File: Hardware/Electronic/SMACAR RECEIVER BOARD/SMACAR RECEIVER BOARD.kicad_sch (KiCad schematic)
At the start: 7 parts, among them J1 M04POLAR, J2 USB_C_Receptacle_USB2.0_14P, U1 ESP32-S3-DevKitC

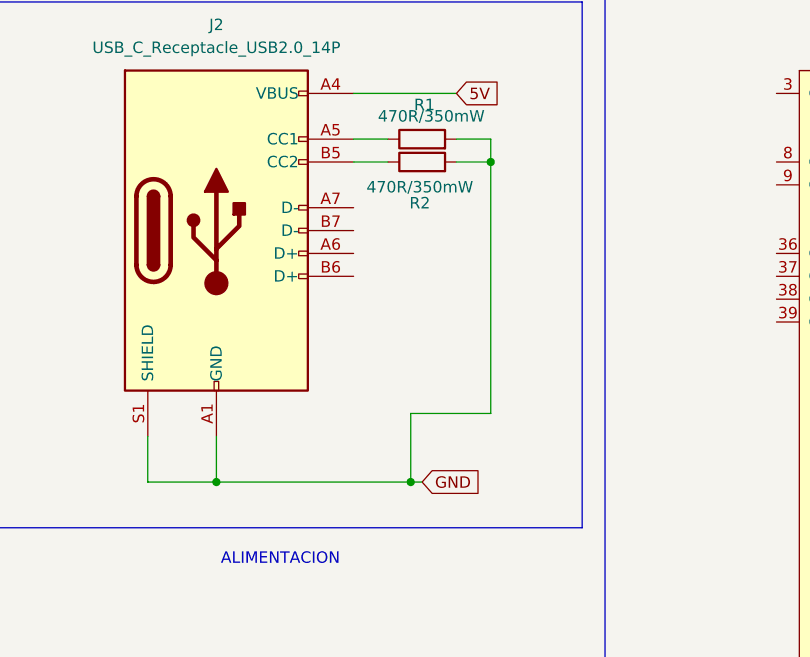
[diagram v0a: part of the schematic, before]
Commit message: arreglos en las conexiones de usb c
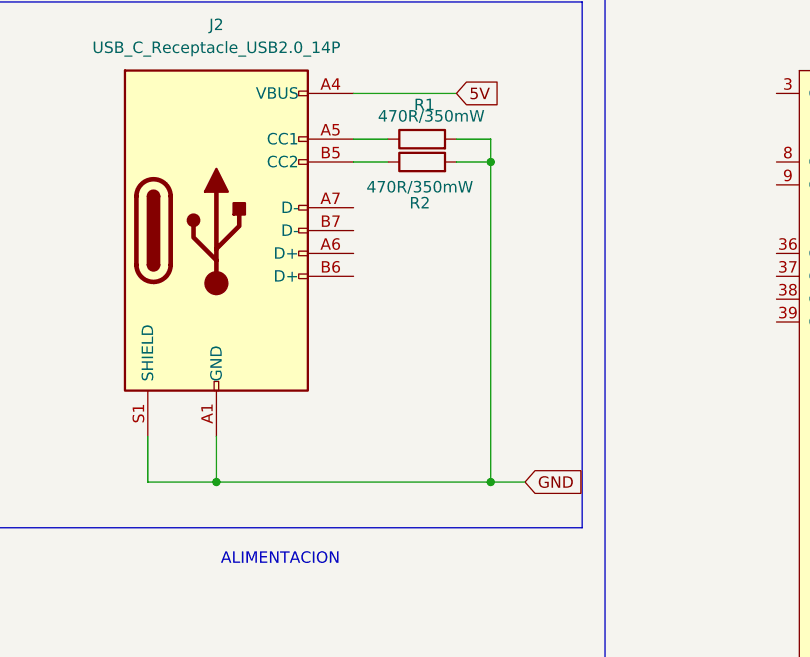
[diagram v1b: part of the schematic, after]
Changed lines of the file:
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@@
+	)
+	(junction
+		(at 86.36 71.12)
+		(diameter 0)
+		(color 0 0 0 0)
 	)
 	(junction
@@
 	)
 	(junction
-		(at 77.47 71.12)
-		(diameter 0)
-		(color 0 0 0 0)
-	)
-	(junction
 		(at 186.69 73.66)
 		(diameter 0)
@@
 	(wire
 		(pts
-			(xy 77.47 71.12) (xy 77.47 63.5)
+			(xy 86.36 35.56) (xy 86.36 71.12)
 		)
 		(stroke
@@
 	(wire
 		(pts
-			(xy 55.88 71.12) (xy 77.47 71.12)
+			(xy 55.88 71.12) (xy 86.36 71.12)
 		)
 		(stroke
@@
 	(wire
 		(pts
-			(xy 77.47 71.12) (xy 78.74 71.12)
-		)
-		(stroke
-			(width 0)
-			(type default)
-		)
-	)
-	(wire
-		(pts
 			(xy 86.36 33.02) (xy 82.55 33.02)
 		)
@@
 	(wire
 		(pts
-			(xy 77.47 63.5) (xy 86.36 63.5)
-		)
-		(stroke
-			(width 0)
-			(type default)
-		)
-	)
-	(wire
-		(pts
 			(xy 144.78 22.86) (xy 144.78 20.32)
 		)
@@
 	(wire
 		(pts
-			(xy 86.36 63.5) (xy 86.36 35.56)
+			(xy 86.36 71.12) (xy 90.17 71.12)
 		)
 		(stroke
@@
 	(global_label "GND"
 		(shape input)
-		(at 78.74 71.12 0)
+		(at 90.17 71.12 0)
 		(fields_autoplaced yes)
 		(effects
@@
 		)
 		(property "Intersheetrefs" "${INTERSHEET_REFS}"
-			(at 85.5957 71.12 0)
+			(at 97.0257 71.12 0)
 			(effects
 				(font

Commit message: TVS
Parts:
- added U2, U3: TVS0500DRV, Package_SON:WSON-6-1EP_2x2mm_P0.65mm_EP1x1.6mm, symbol Power_Protection:TVS0500DRV
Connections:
- net 5V: now also U2.4 (IN), U2.5 (IN), U2.6 (IN)
- net GND: now also U2.1 (GND), U2.2 (GND), U2.3 (GND), U2.7 (GND), U3.1 (GND), U3.2 (GND), U3.3 (GND), U3.7 (GND)
- net at R3.2, R4.2, U1.1 (3V3)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: now also U3.4 (IN), U3.5 (IN), U3.6 (IN)

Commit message: V1.0 Revision
Revision for V1.0 of the project. Includes production files for JLCPCB. Some footprints and schematic symbols were changed.
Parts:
- removed J2: USB_C_Receptacle_USB2.0_14P, Connector_USB:USB_C_Receptacle_GCT_USB4105-xx-A_16P_TopMnt_Horizontal, symbol Connector:USB_C_Receptacle_USB2.0_14P
- removed R1, R2: 470R_0805_350mW, Resistor_SMD:R_0805_2012Metric, symbol PCM_4ms_Resistor:470R_0805_350mW
- removed U2, U3: TVS0500DRV, Package_SON:WSON-6-1EP_2x2mm_P0.65mm_EP1x1.6mm, symbol Power_Protection:TVS0500DRV
- added D1, D2: SMF33A, Diode_SMD:D_SMF, symbol Diode:SMF33A
- added J2: 2137160001, XUNPU TYPEC-306DDW-ARP16:MOLEX_2137160001, symbol XUNPU TYPEC-306DDW-ARP16:2137160001
- added R1_5.1k1, R2_5.1k1: 470R_0805_350mW, Resistor_SMD:R_0805_2012Metric_Pad1.20x1.40mm_HandSolder, symbol PCM_4ms_Resistor:470R_0805_350mW
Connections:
- net GND: now also D1.2 (A2), D2.2 (A2), J2.A1 (GND1), J2.A12 (GND2), J2.B1 (GND3), J2.B12 (GND4), J2.SH1 (SHIELD1), J2.SH2 (SHIELD2), J2.SH3 (SHIELD3), J2.SH4 (SHIELD4)
- net at R3.2, R4.2, U1.1 (3V3)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: now also D2.1 (A1)
- net 5V renamed +5V
- net +5V: now also D1.1 (A1), J2.A4 (VBUS1), J2.A9 (VBUS2), J2.B4 (VBUS3), J2.B9 (VBUS4), R1_5.1k1.2, R2_5.1k1.1
- new net: J2.A5 (CC1), R2_5.1k1.2
- new net: J2.B5 (CC2), R1_5.1k1.1

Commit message: update
PCB Y CODIGO PROTOTIPO
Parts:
- removed D1, D2: SMF33A, Diode_SMD:D_SMF, symbol Diode:SMF33A
- removed J2: 2137160001, XUNPU TYPEC-306DDW-ARP16:MOLEX_2137160001, symbol XUNPU TYPEC-306DDW-ARP16:2137160001
- removed R1_5.1k1, R2_5.1k1: 470R_0805_350mW, Resistor_SMD:R_0805_2012Metric_Pad1.20x1.40mm_HandSolder, symbol PCM_4ms_Resistor:470R_0805_350mW
- added J2: Conn_01x02, Connector_Molex:Molex_KK-254_AE-6410-02A_1x02_P2.54mm_Vertical, symbol SparkFun-Connector:Conn_01x02
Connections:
- net +5V: now also J2.2 (Pin_2)
- net GND: now also J2.1 (Pin_1)
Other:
- moved on the sheet: J1

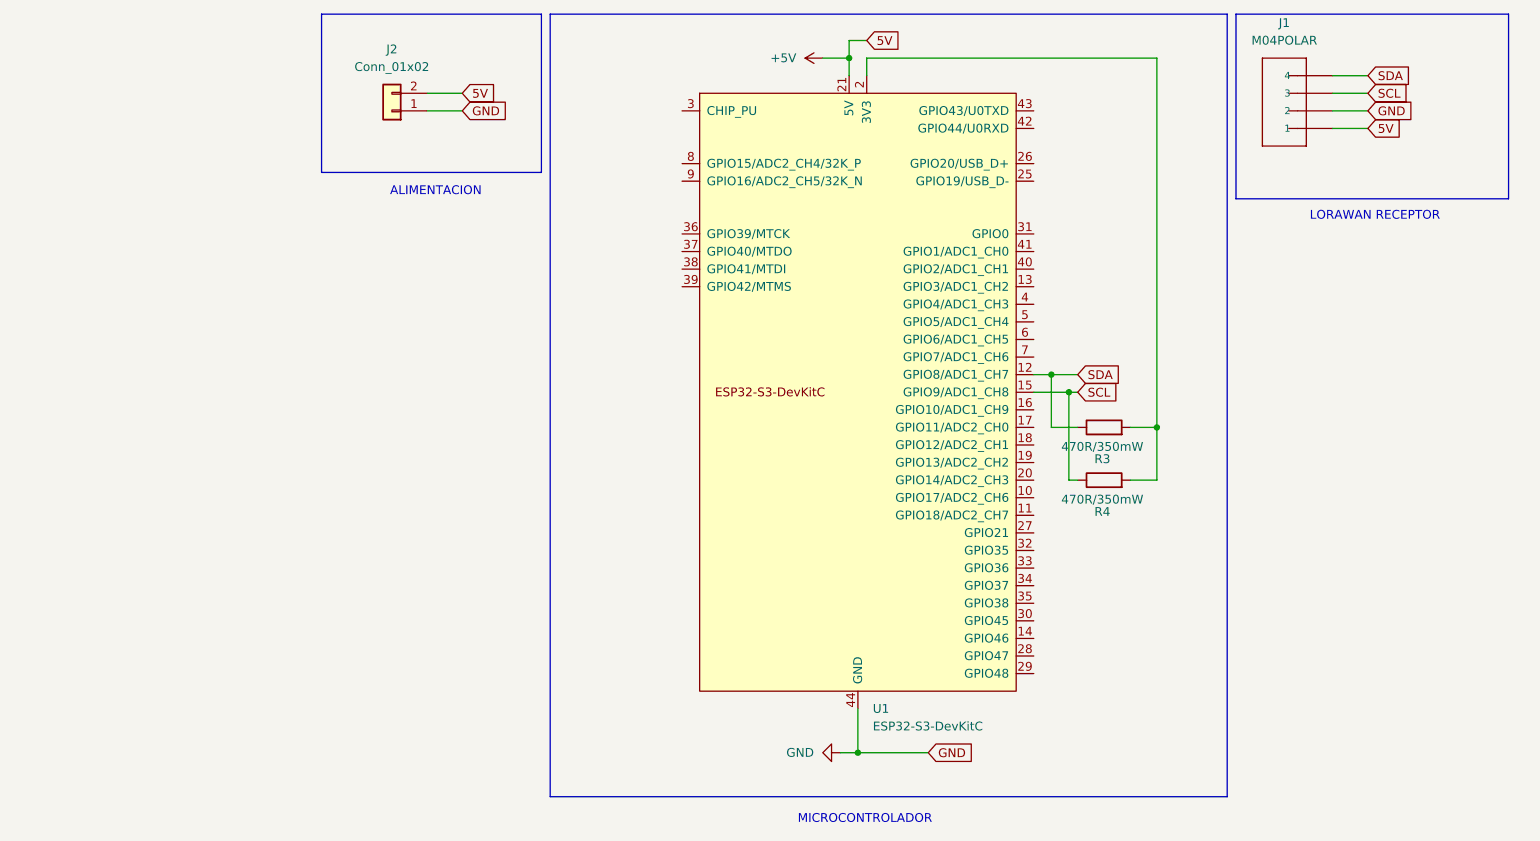
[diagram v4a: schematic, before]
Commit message: PCB RECEPTOR MODIFICADA
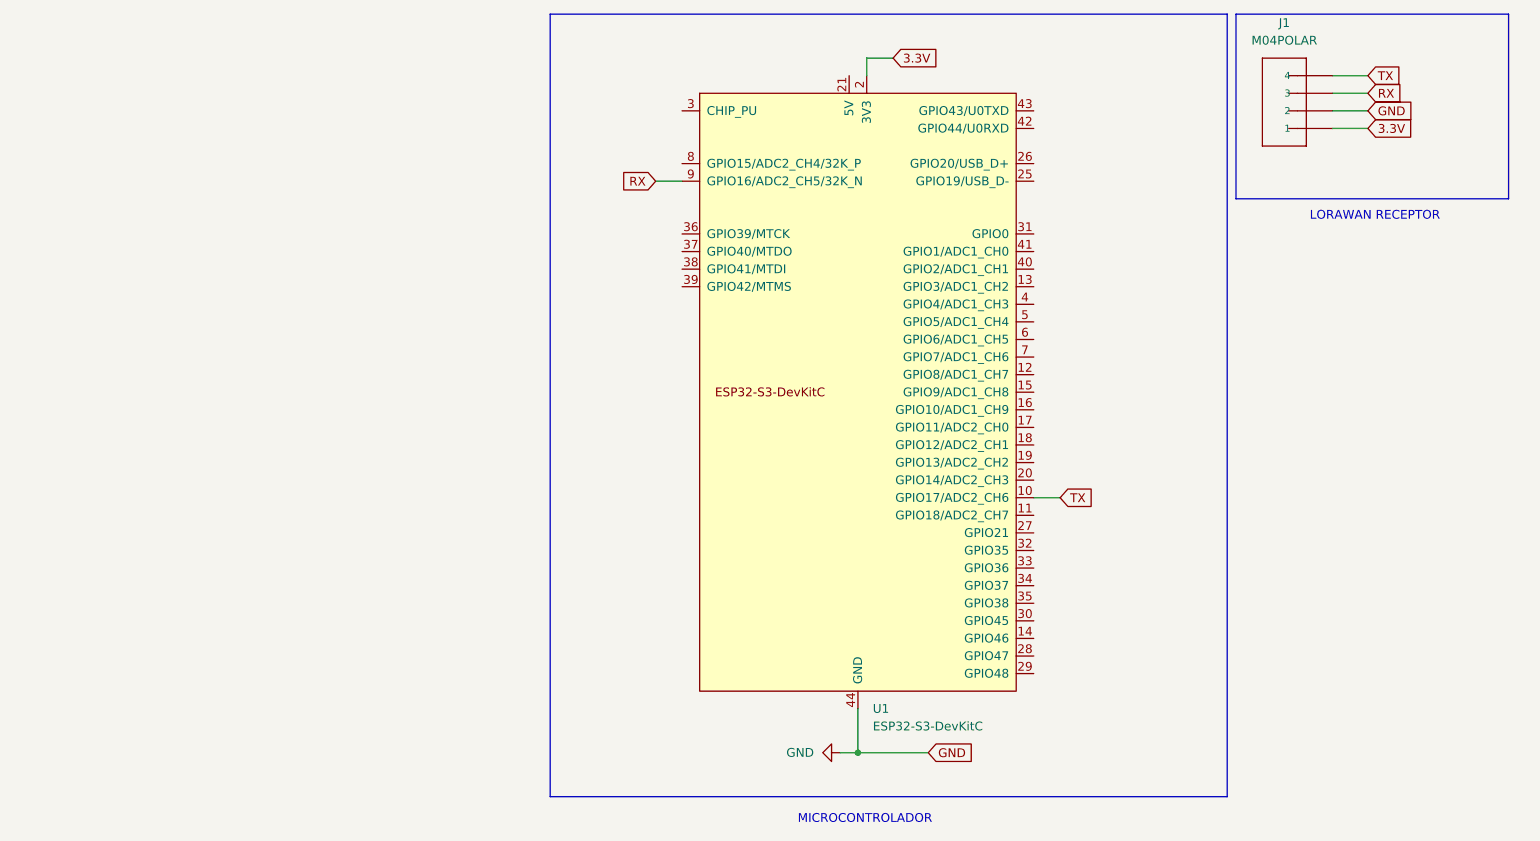
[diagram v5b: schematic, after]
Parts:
- removed J2: Conn_01x02, Connector_Molex:Molex_KK-254_AE-6410-02A_1x02_P2.54mm_Vertical, symbol SparkFun-Connector:Conn_01x02
- removed R3, R4: 470R_0805_350mW, Resistor_SMD:R_0805_2012Metric, symbol PCM_4ms_Resistor:470R_0805_350mW
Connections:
- net 3.3V: now reaches U1.1 (3V3), U1.2 (3V3)
- net 3.3V: now also J1.1
- net TX: now reaches U1.10 (GPIO17/ADC2_CH6)
- net TX: now also J1.4
- net RX: now reaches U1.9 (GPIO16/ADC2_CH5/32K_N)
- net RX: now also J1.3
- net +5V: no longer names the net of U1.21 (5V)
- net +5V: no longer J1.1
- net SCL: no longer names the net of U1.15 (GPIO9/ADC1_CH8)
- net SCL: no longer J1.3
- net SDA: no longer names the net of U1.12 (GPIO8/ADC1_CH7)
- net SDA: no longer J1.4
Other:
- note removed: "ALIMENTACION"
